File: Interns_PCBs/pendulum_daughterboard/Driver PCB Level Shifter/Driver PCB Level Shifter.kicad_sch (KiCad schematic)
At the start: 7 parts, among them J3 DRIVE_GND, J4 DRIVE_5V, J5 3.3V

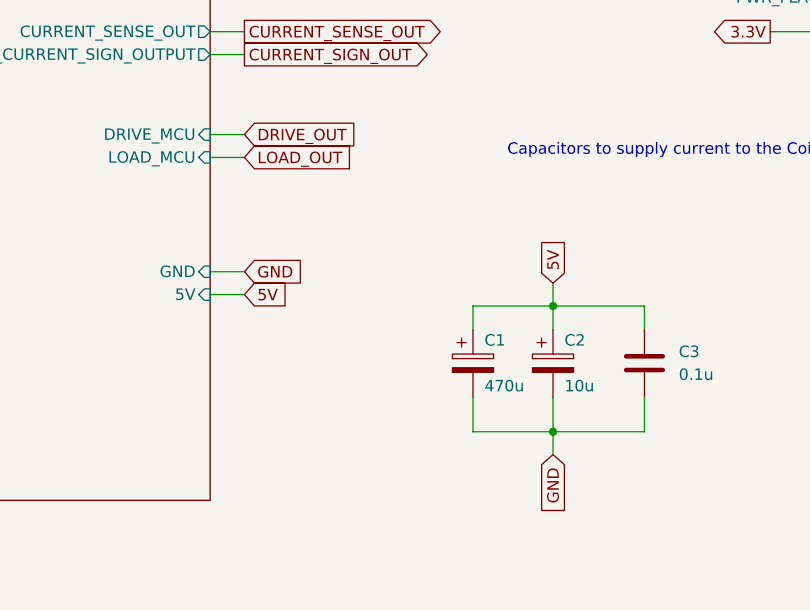
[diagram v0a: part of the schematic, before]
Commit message: Level Shifting Daughterboard
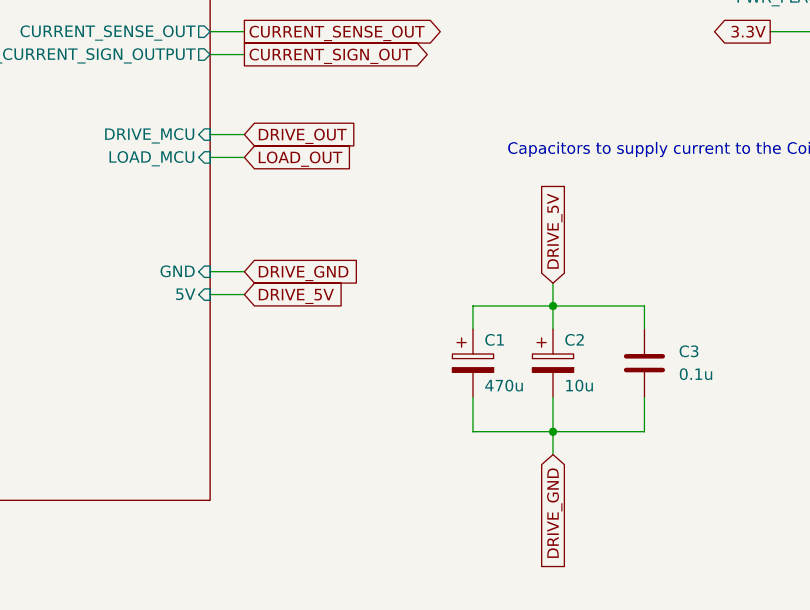
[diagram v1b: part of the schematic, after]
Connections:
- net 5V is gone; now on net DRIVE_5V: C1.1, C2.1, C3.1
- net GND is gone; now on net DRIVE_GND: C1.2, C2.2, C3.2
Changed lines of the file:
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@@
     )
   )
-  (global_label "GND" (shape input) (at 99.06 154.94 0) (fields_autoplaced)
-    (effects (font (size 1.27 1.27)) (justify left))
-    (property "Intersheet References" "${INTERSHEET_REFS}" (id 0) (at 105.3436 154.8606 0)
+  (global_label "DRIVE_GND" (shape input) (at 99.06 154.94 0) (fields_autoplaced)
+    (effects (font (size 1.27 1.27)) (justify left))
+    (property "Intersheet References" "${INTERSHEET_REFS}" (id 0) (at 111.6936 154.8606 0)
       (effects (font (size 1.27 1.27)) (justify left) hide)
     )
@@
     )
   )
-  (global_label "5V" (shape input) (at 99.06 157.48 0) (fields_autoplaced)
-    (effects (font (size 1.27 1.27)) (justify left))
-    (property "Intersheet References" "${INTERSHEET_REFS}" (id 0) (at 103.7712 157.4006 0)
+  (global_label "DRIVE_5V" (shape input) (at 99.06 157.48 0) (fields_autoplaced)
+    (effects (font (size 1.27 1.27)) (justify left))
+    (property "Intersheet References" "${INTERSHEET_REFS}" (id 0) (at 110.1212 157.4006 0)
       (effects (font (size 1.27 1.27)) (justify left) hide)
     )
@@
     )
   )
-  (global_label "GND" (shape input) (at 133.35 175.26 270) (fields_autoplaced)
-    (effects (font (size 1.27 1.27)) (justify right))
-    (property "Intersheet References" "${INTERSHEET_REFS}" (id 0) (at 133.2706 181.5436 90)
+  (global_label "DRIVE_GND" (shape input) (at 133.35 175.26 270) (fields_autoplaced)
+    (effects (font (size 1.27 1.27)) (justify right))
+    (property "Intersheet References" "${INTERSHEET_REFS}" (id 0) (at 133.2706 187.8936 90)
       (effects (font (size 1.27 1.27)) (justify right) hide)
     )
@@
     )
   )
-  (global_label "5V" (shape input) (at 133.35 156.21 90) (fields_autoplaced)
-    (effects (font (size 1.27 1.27)) (justify left))
-    (property "Intersheet References" "${INTERSHEET_REFS}" (id 0) (at 133.2706 151.4988 90)
+  (global_label "DRIVE_5V" (shape input) (at 133.35 156.21 90) (fields_autoplaced)
+    (effects (font (size 1.27 1.27)) (justify left))
+    (property "Intersheet References" "${INTERSHEET_REFS}" (id 0) (at 133.2706 145.1488 90)
       (effects (font (size 1.27 1.27)) (justify left) hide)
     )
@@
     )
     (path "/21780cc4-9565-4c48-acf2-9e239c61d608/ffa549c0-2272-4d9e-a0b7-053a3c5f6dee"
-      (reference "R10") (unit 1) (value "10k") (footprint "")
+      (reference "R10") (unit 1) (value "10k") (footprint "Resistor_SMD:R_0805_2012Metric_Pad1.20x1.40mm_HandSolder")
     )
     (path "/21780cc4-9565-4c48-acf2-9e239c61d608/1f75ba65-1ed3-4376-942e-94d1a5a22140"
-      (reference "R11") (unit 1) (value "10k") (footprint "")
+      (reference "R11") (unit 1) (value "10k") (footprint "Resistor_SMD:R_0805_2012Metric_Pad1.20x1.40mm_HandSolder")
     )
     (path "/21780cc4-9565-4c48-acf2-9e239c61d608/1821cf91-162e-4ca2-91ea-1fe7c94e7ed9"
-      (reference "R12") (unit 1) (value "10k") (footprint "")
+      (reference "R12") (unit 1) (value "10k") (footprint "Resistor_SMD:R_0805_2012Metric_Pad1.20x1.40mm_HandSolder")
     )
     (path "/1a3370a0-6778-4601-bc8e-4c18ed659ac3/8da85c48-5d76-4fcd-8d9c-14f48ce089fa"
@@
     )
     (path "/21780cc4-9565-4c48-acf2-9e239c61d608/4350a4ad-8498-4d4b-8650-6dd7884f5da2"
-      (reference "R14") (unit 1) (value "10k") (footprint "")
+      (reference "R14") (unit 1) (value "10k") (footprint "Resistor_SMD:R_0805_2012Metric_Pad1.20x1.40mm_HandSolder")
     )
     (path "/1a3370a0-6778-4601-bc8e-4c18ed659ac3/3900ff34-bdaf-4e75-a513-7c221e9e1b48"
